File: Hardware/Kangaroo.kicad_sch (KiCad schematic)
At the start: 8 parts, among them U1 LM2588S-ADJ

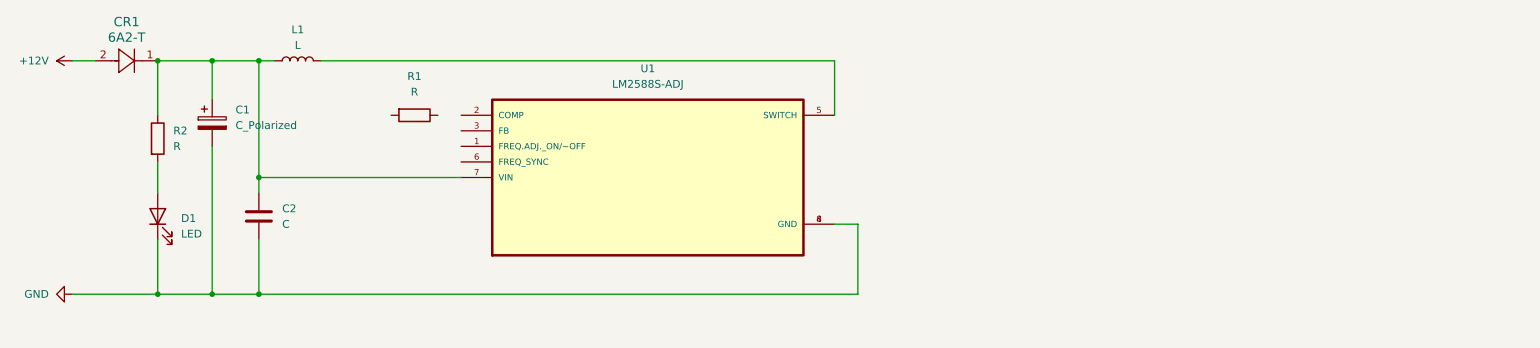
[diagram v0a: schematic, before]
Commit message: Completed Initial Schematic
LM2588-ADJ IC with 6 pin socket
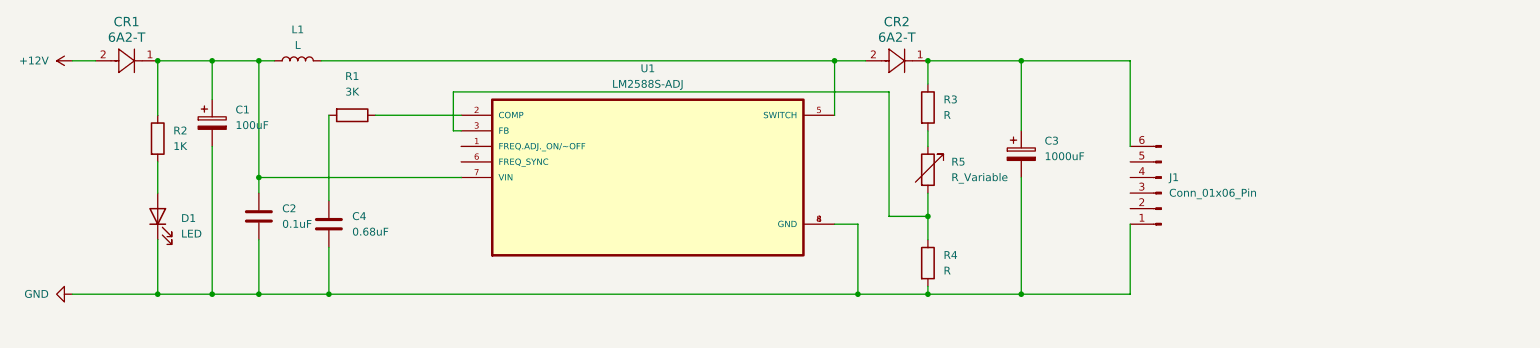
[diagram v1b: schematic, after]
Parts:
- added C3: 1000uF, symbol Device:C_Polarized
- added C4: 0.68uF, symbol Device:C
- added CR2: 6A2-T, R-6_DIO, symbol 2024-02-09_11-49-23:6A2-T
- added J1: Conn_01x06_Pin, symbol Connector:Conn_01x06_Pin
- added R3, R4: R, symbol Device:R
- added R5: R_Variable, symbol Device:R_Variable
- C1: value C_Polarized -> 100uF
- C2: value C -> 0.1uF
- R1: value R -> 3K
- R2: value R -> 1K
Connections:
- net GND: now also C3.2, C4.2, J1.1 (Pin_1), R4.2
- net at L1.2, U1.5 (SWITCH): now also CR2.2
- net at U1.2 (COMP): now also R1.1
- net at U1.3 (FB): now also R4.1, R5.2
- net at R1.2: now also C4.1
- new net: C3.1, CR2.1, J1.6 (Pin_6), R3.1
- new net: R3.2, R5.1
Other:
- moved on the sheet: R1

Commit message: 6 Pin Socket Change
Schematic Finished - in theory
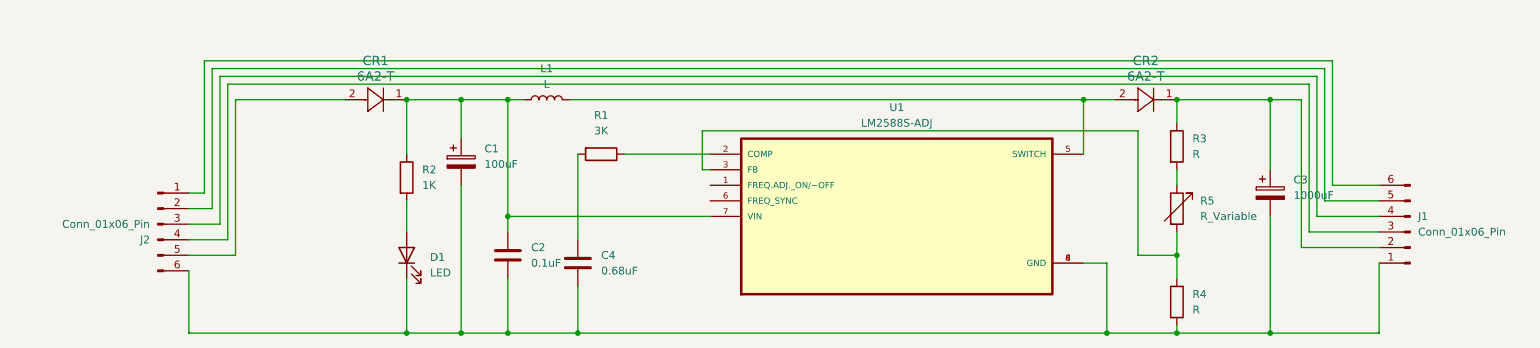
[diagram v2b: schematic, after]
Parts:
- added J2: Conn_01x06_Pin, symbol Connector:Conn_01x06_Pin
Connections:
- net at C3.1, CR2.1, R3.1: now also J1.2 (Pin_2); no longer J1.6 (Pin_6)
- net at J1.3 (Pin_3): now also J2.4 (Pin_4)
- net at J1.4 (Pin_4): now also J2.3 (Pin_3)
- net at J1.5 (Pin_5): now also J2.2 (Pin_2)
- net +12V: no longer names the net of CR1.2
- net +12V: now also J2.5 (Pin_5)
- net GND: no longer names the net of C1.2, C2.2, C3.2, C4.2, D1.1 (K), J1.1 (Pin_1), R4.2, U1.4 (GND), U1.8 (GND)
- net GND: now also J2.6 (Pin_6)
- new net: J1.6 (Pin_6), J2.1 (Pin_1)
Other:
- moved on the sheet: C1, C2, C3, C4, CR1, CR2, D1, J1, L1, R1, R2, R3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

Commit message: Test PCB Design
Tested PCB design of Kangaroo - proper footprints need to be verified with Shiven.
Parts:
- C1, C2, C3, C4: footprint (none) -> Capacitor_SMD:C_3640_9110Metric
- D1: footprint (none) -> LED_SMD:LED_2512_6332Metric
- J1, J2: footprint (none) -> Connector_PinSocket_1.27mm:PinSocket_1x06_P1.27mm_Vertical
- L1: footprint (none) -> Inductor_THT:L_Axial_L20.0mm_D8.0mm_P7.62mm_Vertical
- R1, R2, R3, R4: footprint (none) -> Resistor_SMD:R_4020_10251Metric
- R5: footprint (none) -> Varistor:RV_Disc_D9mm_W3.9mm_P5mm
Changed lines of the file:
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@@
       (effects (font (size 1.27 1.27)) (justify left))
     )
-    (property "Footprint" "" (at 94.9452 95.25 0)
+    (property "Footprint" "Capacitor_SMD:C_3640_9110Metric" (at 94.9452 95.25 0)
       (effects (font (size 1.27 1.27)) hide)
     )
@@
       (effects (font (size 1.27 1.27)) (justify right))
     )
-    (property "Footprint" "" (at 85.09 106.68 0)
+    (property "Footprint" "LED_SMD:LED_2512_6332Metric" (at 85.09 106.68 0)
       (effects (font (size 1.27 1.27)) hide)
     )
@@
       (effects (font (size 1.27 1.27)))
     )
-    (property "Footprint" "" (at 107.95 81.28 0)
+    (property "Footprint" "Inductor_THT:L_Axial_L20.0mm_D8.0mm_P7.62mm_Vertical" (at 107.95 81.28 0)
       (effects (font (size 1.27 1.27)) hide)
     )
@@
       (effects (font (size 1.27 1.27)) (justify left))
     )
-    (property "Footprint" "" (at 113.9952 111.76 0)
+    (property "Footprint" "Capacitor_SMD:C_3640_9110Metric" (at 113.9952 111.76 0)
       (effects (font (size 1.27 1.27)) hide)
     )
@@
       (effects (font (size 1.27 1.27)) (justify left))
     )
-    (property "Footprint" "" (at 209.042 88.9 90)
+    (property "Footprint" "Resistor_SMD:R_4020_10251Metric" (at 209.042 88.9 90)
       (effects (font (size 1.27 1.27)) hide)
     )
@@
       (effects (font (size 1.27 1.27)) (justify right))
     )
-    (property "Footprint" "" (at 248.92 102.87 0)
+    (property "Footprint" "Connector_PinSocket_1.27mm:PinSocket_1x06_P1.27mm_Vertical" (at 248.92 102.87 0)
       (effects (font (size 1.27 1.27)) hide)
     )
@@
       (effects (font (size 1.27 1.27)) (justify left))
     )
-    (property "Footprint" "" (at 209.042 99.06 90)
+    (property "Footprint" "Varistor:RV_Disc_D9mm_W3.9mm_P5mm" (at 209.042 99.06 90)
       (effects (font (size 1.27 1.27)) hide)
     )
@@
       (effects (font (size 1.27 1.27)))
     )
-    (property "Footprint" "" (at 116.84 88.392 90)
+    (property "Footprint" "Resistor_SMD:R_4020_10251Metric" (at 116.84 88.392 90)
       (effects (font (size 1.27 1.27)) hide)
     )
@@
       (effects (font (size 1.27 1.27)) (justify right))
     )
-    (property "Footprint" "" (at 44.45 101.6 0)
+    (property "Footprint" "Connector_PinSocket_1.27mm:PinSocket_1x06_P1.27mm_Vertical" (at 44.45 101.6 0)
       (effects (font (size 1.27 1.27)) hide)
     )
@@
       (effects (font (size 1.27 1.27)) (justify left))
     )
-    (property "Footprint" "" (at 209.042 114.3 90)
+    (property "Footprint" "Resistor_SMD:R_4020_10251Metric" (at 209.042 114.3 90)
       (effects (font (size 1.27 1.27)) hide)
     )
@@
       (effects (font (size 1.27 1.27)) (justify left))
     )
-    (property "Footprint" "" (at 227.0252 100.33 0)
+    (property "Footprint" "Capacitor_SMD:C_3640_9110Metric" (at 227.0252 100.33 0)
       (effects (font (size 1.27 1.27)) hide)
     )
@@
       (effects (font (size 1.27 1.27)) (justify left))
     )
-    (property "Footprint" "" (at 102.5652 110.49 0)
+    (property "Footprint" "Capacitor_SMD:C_3640_9110Metric" (at 102.5652 110.49 0)
       (effects (font (size 1.27 1.27)) hide)
     )
@@
       (effects (font (size 1.27 1.27)) (justify left))
     )
-    (property "Footprint" "" (at 83.312 93.98 90)
-      (effects (font (size 1.27 1.27)) hide)
-    )
+    (property "Footprint" "Resistor_SMD:R_4020_10251Metric" (at 83.312 93.98 90)
+      (effects (font (size 1.27 1.27)) hide)
+    )

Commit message: Changed Schematic  & Footprints Symbols Added
New correct footprints added
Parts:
- removed R3: R, Resistor_SMD:R_4020_10251Metric, symbol Device:R
- removed R5: R_Variable, Varistor:RV_Disc_D9mm_W3.9mm_P5mm, symbol Device:R_Variable
- added R1: 24.5K, Resistor_SMD:R_0402_1005Metric, symbol Device:R
- C1, C3: footprint Capacitor_SMD:C_3640_9110Metric -> Capacitor_SMD:C_0201_0603Metric
- C2: footprint Capacitor_SMD:C_3640_9110Metric -> Capacitor_SMD:C_0402_1005Metric
- C4: footprint Capacitor_SMD:C_3640_9110Metric -> Resistor_SMD:R_0805_2012Metric
- D1: footprint LED_SMD:LED_2512_6332Metric -> LED_SMD:LED_0402_1005Metric
- J1, J2: footprint Connector_PinSocket_1.27mm:PinSocket_1x06_P1.27mm_Vertical -> iclr:Molex_Mini-Fit_Jr_5569-06A2_2x03_P4.20mm_Horizontal_No_Mounting_Holes
- R2: renamed from R4; value R -> 350; footprint Resistor_SMD:R_4020_10251Metric -> Resistor_SMD:R_0402_1005Metric
- R4: renamed from R1; footprint Resistor_SMD:R_4020_10251Metric -> Resistor_SMD:R_0402_1005Metric
- R5: renamed from R2; footprint Resistor_SMD:R_4020_10251Metric -> Resistor_SMD:R_0402_1005Metric
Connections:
- net at C3.1, CR2.1, J1.2 (Pin_2): now also R1.1
- net at R2.1, U1.3 (FB): now also R1.2
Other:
- moved on the sheet: C3

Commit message: Specific components added
Inductor 50uH 5A slim, Diodes (Rectifying and SBR1045)
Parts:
- removed CR1: 6A2-T, R-6_DIO, symbol 2024-02-09_11-49-23:6A2-T
- removed L1: L, Inductor_THT:L_Axial_L20.0mm_D8.0mm_P7.62mm_Vertical, symbol Device:L
- added D2: B540C-13-F, iclr:DIOM6959X245N, symbol iclr:B540C-13-F
- added L1: P0848NL, iclr:P0848NL, symbol iclr:P0848NL
- CR2: value 6A2-T -> SBR1045; footprint R-6_DIO -> iclr:DPAK228P990X239-4N
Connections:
- net at C1.1, C2.1, R5.1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: now also D2.C, L1.1
- net at J2.5 (Pin_5): now also D2.A
- net at CR2.2, U1.5 (SWITCH): now also L1.2
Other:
- company: (none) -> IMPERIAL COLLEGE LONDON
- title: (none) -> Kangaroo Boost Board
